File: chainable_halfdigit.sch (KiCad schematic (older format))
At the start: 42 parts, among them J1 Conn_01x03, J2 Conn_01x03

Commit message: Added more LEDs and created PCB
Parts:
- added C21, C22, C23: 100nF, Capacitors_SMD:C_0603, symbol C
- added LED21, LED22, LED23: WS2812B, WS2812B:WS2812B_data-bridgeable, symbol WS2812B
- C1, C10, C11, C12, C13, C14, C15, C16, C17, C18, C19, C2, C20, C3, C4, C5, C6, C7, C8, C9: footprint (none) -> Capacitors_SMD:C_0603
- J1, J2: footprint (none) -> Pin_Headers:Pin_Header_Straight_1x03_Pitch2.54mm
- LED1, LED10, LED11, LED12, LED13, LED14, LED15, LED16, LED17, LED18, LED19, LED2, LED20, LED3, LED4, LED5, LED6, LED7, LED8, LED9: footprint (none) -> WS2812B:WS2812B_data-bridgeable
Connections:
- net +5V: now also C21.1, C22.1, C23.1, LED21.1 (VCC), LED22.1 (VCC), LED23.1 (VCC)
- net DATA_OUT: now also LED23.2 (DOUT); no longer LED20.2 (DOUT)
- net GND: now also C21.2, C22.2, C23.2, LED21.3 (GND), LED22.3 (GND), LED23.3 (GND)
- new net: LED20.2 (DOUT), LED21.4 (DIN)
- new net: LED21.2 (DOUT), LED22.4 (DIN)
- new net: LED22.2 (DOUT), LED23.4 (DIN)
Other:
- moved on the sheet: C1, C10, C11, C12, C13, C14, C15, C16, C17, C18, C19, C2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

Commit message: Made pretty lib as local. Added 3D model to leds.
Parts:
- LED1, LED10, LED11, LED12, LED13, LED14, LED15, LED16, LED17, LED18, LED19, LED2, LED20, LED21, LED22, LED23, LED3, LED4, LED5, LED6, LED7, LED8, LED9: footprint WS2812B:WS2812B_data-bridgeable -> lib_fp:WS2812B_data-bridgeable
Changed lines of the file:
@@
 F 0 "LED1" H 1950 1050 60  0000 C CNN
 F 1 "WS2812B" H 1950 1850 60  0000 C CNN
-F 2 "WS2812B:WS2812B_data-bridgeable" V 1900 1450 60  0001 C CNN
+F 2 "lib_fp:WS2812B_data-bridgeable" V 1900 1450 60  0001 C CNN
 F 3 "" V 1900 1450 60  0000 C CNN
 	1    1950 1450
@@
 $EndComp
 $Comp
-L +5V #PWR2
+L +5V #PWR01
 U 1 1 5A021F2B
 P 1850 2250
-F 0 "#PWR2" H 1850 2100 50  0001 C CNN
+F 0 "#PWR01" H 1850 2100 50  0001 C CNN
 F 1 "+5V" H 1850 2390 50  0000 C CNN
 F 2 "" H 1850 2250 50  0001 C CNN
@@
 $EndComp
 $Comp
-L GND #PWR1
+L GND #PWR02
 U 1 1 5A021F41
 P 1450 750
-F 0 "#PWR1" H 1450 500 50  0001 C CNN
+F 0 "#PWR02" H 1450 500 50  0001 C CNN
 F 1 "GND" H 1450 600 50  0000 C CNN
 F 2 "" H 1450 750 50  0001 C CNN
@@
 F 0 "LED2" H 3150 1050 60  0000 C CNN
 F 1 "WS2812B" H 3150 1850 60  0000 C CNN
-F 2 "WS2812B:WS2812B_data-bridgeable" V 3100 1450 60  0001 C CNN
+F 2 "lib_fp:WS2812B_data-bridgeable" V 3100 1450 60  0001 C CNN
 F 3 "" V 3100 1450 60  0000 C CNN
 	1    3150 1450
@@
 F 0 "LED3" H 4350 1050 60  0000 C CNN
 F 1 "WS2812B" H 4350 1850 60  0000 C CNN
-F 2 "WS2812B:WS2812B_data-bridgeable" V 4300 1450 60  0001 C CNN
+F 2 "lib_fp:WS2812B_data-bridgeable" V 4300 1450 60  0001 C CNN
 F 3 "" V 4300 1450 60  0000 C CNN
 	1    4350 1450
@@
 F 0 "LED4" H 5550 1050 60  0000 C CNN
 F 1 "WS2812B" H 5550 1850 60  0000 C CNN
-F 2 "WS2812B:WS2812B_data-bridgeable" V 5500 1450 60  0001 C CNN
+F 2 "lib_fp:WS2812B_data-bridgeable" V 5500 1450 60  0001 C CNN
 F 3 "" V 5500 1450 60  0000 C CNN
 	1    5550 1450
@@
 F 0 "LED5" H 6750 1050 60  0000 C CNN
 F 1 "WS2812B" H 6750 1850 60  0000 C CNN
-F 2 "WS2812B:WS2812B_data-bridgeable" V 6700 1450 60  0001 C CNN
+F 2 "lib_fp:WS2812B_data-bridgeable" V 6700 1450 60  0001 C CNN
 F 3 "" V 6700 1450 60  0000 C CNN
 	1    6750 1450
@@
 F 0 "LED6" H 7950 1050 60  0000 C CNN
 F 1 "WS2812B" H 7950 1850 60  0000 C CNN
-F 2 "WS2812B:WS2812B_data-bridgeable" V 7900 1450 60  0001 C CNN
+F 2 "lib_fp:WS2812B_data-bridgeable" V 7900 1450 60  0001 C CNN
 F 3 "" V 7900 1450 60  0000 C CNN
 	1    7950 1450
@@
 F 0 "LED7" H 9150 1050 60  0000 C CNN
 F 1 "WS2812B" H 9150 1850 60  0000 C CNN
-F 2 "WS2812B:WS2812B_data-bridgeable" V 9100 1450 60  0001 C CNN
+F 2 "lib_fp:WS2812B_data-bridgeable" V 9100 1450 60  0001 C CNN
 F 3 "" V 9100 1450 60  0000 C CNN
 	1    9150 1450
@@
 F 0 "LED8" H 10350 1050 60  0000 C CNN
 F 1 "WS2812B" H 10350 1850 60  0000 C CNN
-F 2 "WS2812B:WS2812B_data-bridgeable" V 10300 1450 60  0001 C CNN
+F 2 "lib_fp:WS2812B_data-bridgeable" V 10300 1450 60  0001 C CNN
 F 3 "" V 10300 1450 60  0000 C CNN
 	1    10350 1450
@@
 F 0 "LED9" H 1950 3000 60  0000 C CNN
 F 1 "WS2812B" H 1950 3800 60  0000 C CNN
-F 2 "WS2812B:WS2812B_data-bridgeable" V 1900 3400 60  0001 C CNN
+F 2 "lib_fp:WS2812B_data-bridgeable" V 1900 3400 60  0001 C CNN
 F 3 "" V 1900 3400 60  0000 C CNN
 	1    1950 3400
@@
 F 0 "LED10" H 3150 3000 60  0000 C CNN
 F 1 "WS2812B" H 3150 3800 60  0000 C CNN
-F 2 "WS2812B:WS2812B_data-bridgeable" V 3100 3400 60  0001 C CNN
+F 2 "lib_fp:WS2812B_data-bridgeable" V 3100 3400 60  0001 C CNN
 F 3 "" V 3100 3400 60  0000 C CNN
 	1    3150 3400
@@
 F 0 "LED11" H 4350 3000 60  0000 C CNN
 F 1 "WS2812B" H 4350 3800 60  0000 C CNN
-F 2 "WS2812B:WS2812B_data-bridgeable" V 4300 3400 60  0001 C CNN
+F 2 "lib_fp:WS2812B_data-bridgeable" V 4300 3400 60  0001 C CNN
 F 3 "" V 4300 3400 60  0000 C CNN
 	1    4350 3400
@@
 F 0 "LED12" H 5550 3000 60  0000 C CNN
 F 1 "WS2812B" H 5550 3800 60  0000 C CNN
-F 2 "WS2812B:WS2812B_data-bridgeable" V 5500 3400 60  0001 C CNN
+F 2 "lib_fp:WS2812B_data-bridgeable" V 5500 3400 60  0001 C CNN
 F 3 "" V 5500 3400 60  0000 C CNN
 	1    5550 3400
@@
 F 0 "LED13" H 6750 3000 60  0000 C CNN
 F 1 "WS2812B" H 6750 3800 60  0000 C CNN
-F 2 "WS2812B:WS2812B_data-bridgeable" V 6700 3400 60  0001 C CNN
+F 2 "lib_fp:WS2812B_data-bridgeable" V 6700 3400 60  0001 C CNN
 F 3 "" V 6700 3400 60  0000 C CNN
 	1    6750 3400
@@
 F 0 "LED14" H 7950 3000 60  0000 C CNN
 F 1 "WS2812B" H 7950 3800 60  0000 C CNN
-F 2 "WS2812B:WS2812B_data-bridgeable" V 7900 3400 60  0001 C CNN
+F 2 "lib_fp:WS2812B_data-bridgeable" V 7900 3400 60  0001 C CNN
 F 3 "" V 7900 3400 60  0000 C CNN
 	1    7950 3400
@@
 F 0 "LED15" H 9150 3000 60  0000 C CNN
 F 1 "WS2812B" H 9150 3800 60  0000 C CNN
-F 2 "WS2812B:WS2812B_data-bridgeable" V 9100 3400 60  0001 C CNN
+F 2 "lib_fp:WS2812B_data-bridgeable" V 9100 3400 60  0001 C CNN
 F 3 "" V 9100 3400 60  0000 C CNN
 	1    9150 3400
@@
 F 0 "LED16" H 10350 3000 60  0000 C CNN
 F 1 "WS2812B" H 10350 3800 60  0000 C CNN
-F 2 "WS2812B:WS2812B_data-bridgeable" V 10300 3400 60  0001 C CNN
+F 2 "lib_fp:WS2812B_data-bridgeable" V 10300 3400 60  0001 C CNN
 F 3 "" V 10300 3400 60  0000 C CNN
 	1    10350 3400
@@
 F 0 "LED17" H 1950 4800 60  0000 C CNN
 F 1 "WS2812B" H 1950 5600 60  0000 C CNN
-F 2 "WS2812B:WS2812B_data-bridgeable" V 1900 5200 60  0001 C CNN
+F 2 "lib_fp:WS2812B_data-bridgeable" V 1900 5200 60  0001 C CNN
 F 3 "" V 1900 5200 60  0000 C CNN
 	1    1950 5200
@@
 F 0 "LED18" H 3150 4800 60  0000 C CNN
 F 1 "WS2812B" H 3150 5600 60  0000 C CNN
-F 2 "WS2812B:WS2812B_data-bridgeable" V 3100 5200 60  0001 C CNN
+F 2 "lib_fp:WS2812B_data-bridgeable" V 3100 5200 60  0001 C CNN
 F 3 "" V 3100 5200 60  0000 C CNN
 	1    3150 5200
@@
 F 0 "LED19" H 4350 4800 60  0000 C CNN
 F 1 "WS2812B" H 4350 5600 60  0000 C CNN
-F 2 "WS2812B:WS2812B_data-bridgeable" V 4300 5200 60  0001 C CNN
+F 2 "lib_fp:WS2812B_data-bridgeable" V 4300 5200 60  0001 C CNN
 F 3 "" V 4300 5200 60  0000 C CNN
 	1    4350 5200
@@
 F 0 "LED20" H 5550 4800 60  0000 C CNN
 F 1 "WS2812B" H 5550 5600 60  0000 C CNN
-F 2 "WS2812B:WS2812B_data-bridgeable" V 5500 5200 60  0001 C CNN
+F 2 "lib_fp:WS2812B_data-bridgeable" V 5500 5200 60  0001 C CNN
 F 3 "" V 5500 5200 60  0000 C CNN
 	1    5550 5200
@@
 DATA_INOUT_2
 $Comp
-L PWR_FLAG #FLG1
+L PWR_FLAG #FLG03
 U 1 1 5A02F033
 P 2650 750
-F 0 "#FLG1" H 2650 825 50  0001 C CNN
+F 0 "#FLG03" H 2650 825 50  0001 C CNN
 F 1 "PWR_FLAG" H 2650 900 50  0000 C CNN
 F 2 "" H 2650 750 50  0001 C CNN
@@
 $EndComp
 $Comp
-L PWR_FLAG #FLG2
+L PWR_FLAG #FLG04
 U 1 1 5A02F073
 P 1450 2250
-F 0 "#FLG2" H 1450 2325 50  0001 C CNN
+F 0 "#FLG04" H 1450 2325 50  0001 C CNN
 F 1 "PWR_FLAG" H 1450 2400 50  0000 C CNN
 F 2 "" H 1450 2250 50  0001 C CNN
@@
 F 0 "LED21" H 6750 4800 60  0000 C CNN
 F 1 "WS2812B" H 6750 5600 60  0000 C CNN
-F 2 "WS2812B:WS2812B_data-bridgeable" V 6700 5200 60  0001 C CNN
+F 2 "lib_fp:WS2812B_data-bridgeable" V 6700 5200 60  0001 C CNN
 F 3 "" V 6700 5200 60  0000 C CNN
 	1    6750 5200
@@
 F 0 "LED22" H 7950 4800 60  0000 C CNN
 F 1 "WS2812B" H 7950 5600 60  0000 C CNN
-F 2 "WS2812B:WS2812B_data-bridgeable" V 7900 5200 60  0001 C CNN
+F 2 "lib_fp:WS2812B_data-bridgeable" V 7900 5200 60  0001 C CNN
 F 3 "" V 7900 5200 60  0000 C CNN
 	1    7950 5200
@@
 F 0 "LED23" H 9150 4800 60  0000 C CNN
 F 1 "WS2812B" H 9150 5600 60  0000 C CNN
-F 2 "WS2812B:WS2812B_data-bridgeable" V 9100 5200 60  0001 C CNN
+F 2 "lib_fp:WS2812B_data-bridgeable" V 9100 5200 60  0001 C CNN
 F 3 "" V 9100 5200 60  0000 C CNN
 	1    9150 5200

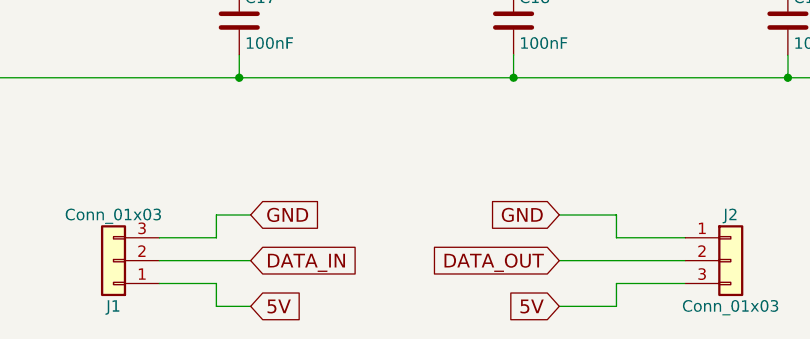
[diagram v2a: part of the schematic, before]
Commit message: Reverse 5V and DATA to avoid circuit damage when reversing connector.
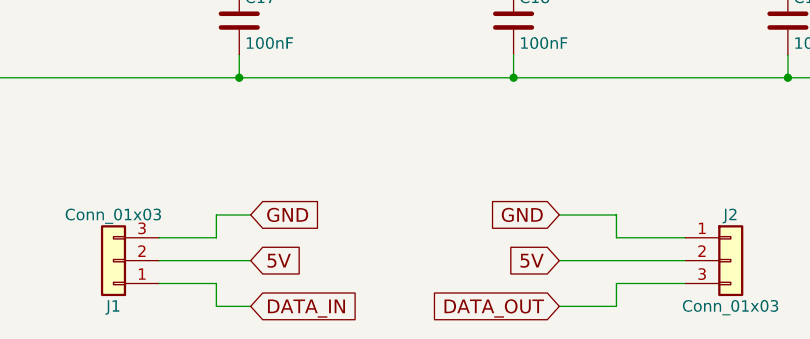
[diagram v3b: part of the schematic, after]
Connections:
- net +5V: now also J1.2 (Pin_2), J2.2 (Pin_2); no longer J1.1 (Pin_1), J2.3 (Pin_3)
- net DATA_IN: now also J1.1 (Pin_1); no longer J1.2 (Pin_2)
- net DATA_OUT: now also J2.3 (Pin_3); no longer J2.2 (Pin_2)
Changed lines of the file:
@@
 Text GLabel 2500 6850 2    60   Input ~ 0
 GND
+Text GLabel 2500 7050 2    60   Input ~ 0
+5V
 Text GLabel 2500 7250 2    60   Input ~ 0
-5V
-Text GLabel 2500 7050 2    60   Input ~ 0
 DATA_IN
 Text GLabel 1150 750  0    60   Input ~ 0
@@
 Text GLabel 3850 6850 0    60   Input ~ 0
 GND
+Text GLabel 3850 7250 0    60   Input ~ 0
+DATA_OUT
 Text GLabel 3850 7050 0    60   Input ~ 0
-DATA_OUT
-Text GLabel 3850 7250 0    60   Input ~ 0
 5V
 Text GLabel 1100 2850 0    60   Input ~ 0

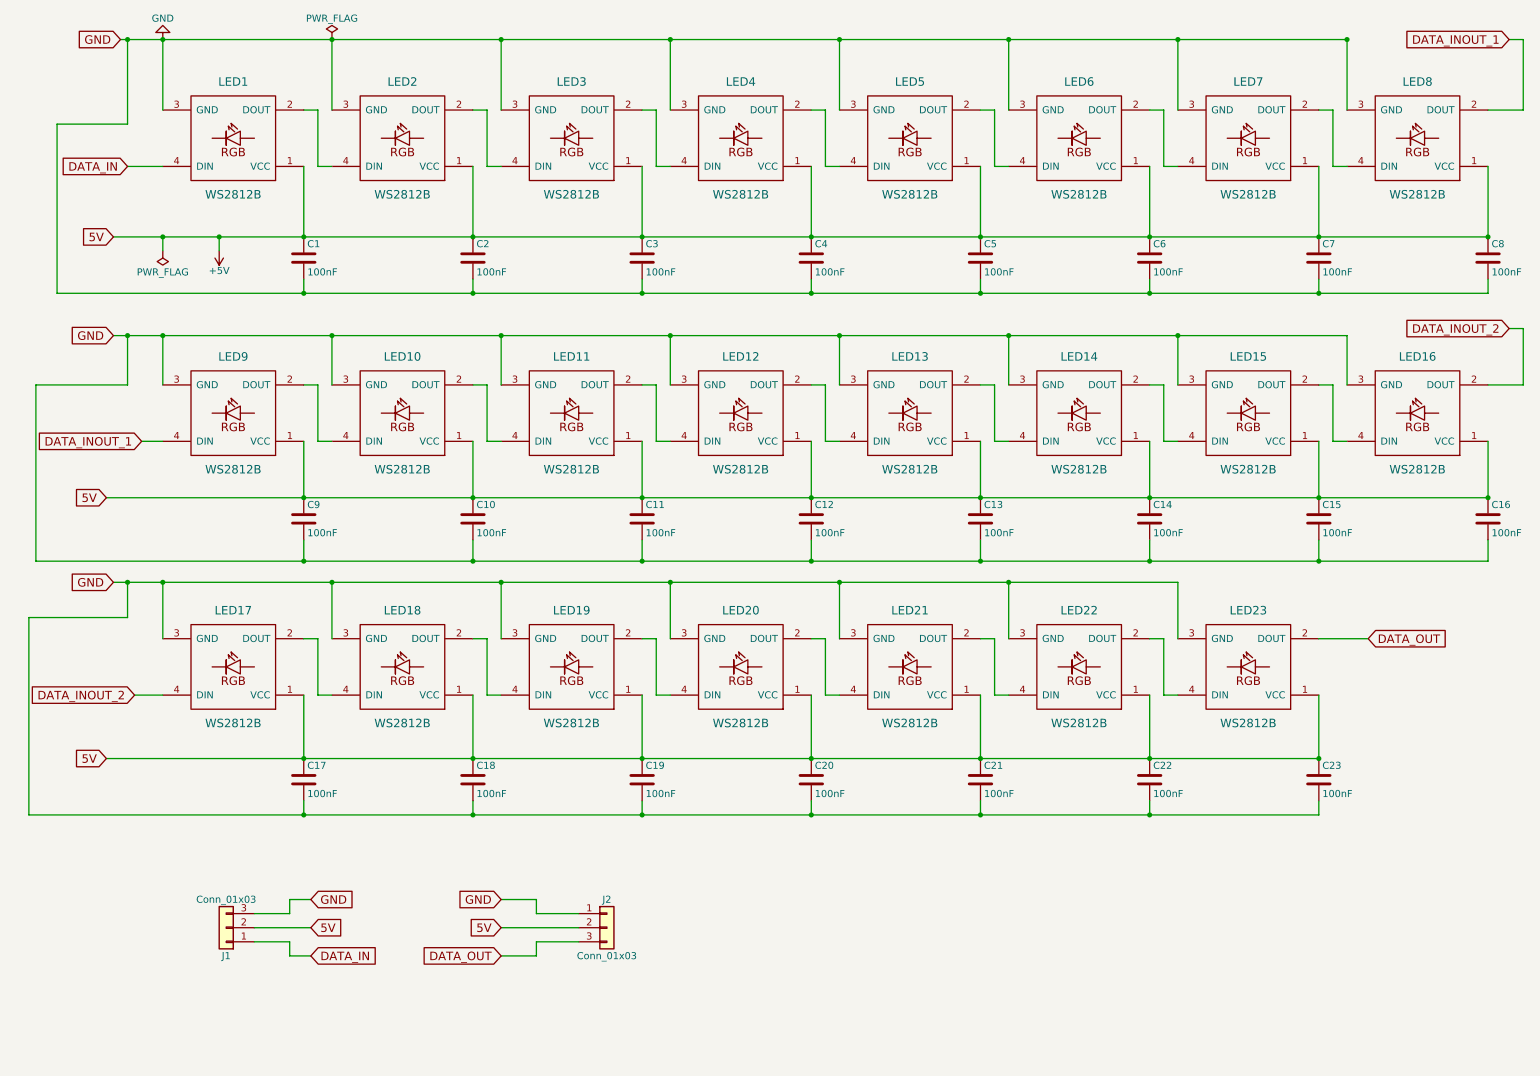
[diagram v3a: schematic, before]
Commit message: Added Arduino Nano footprint
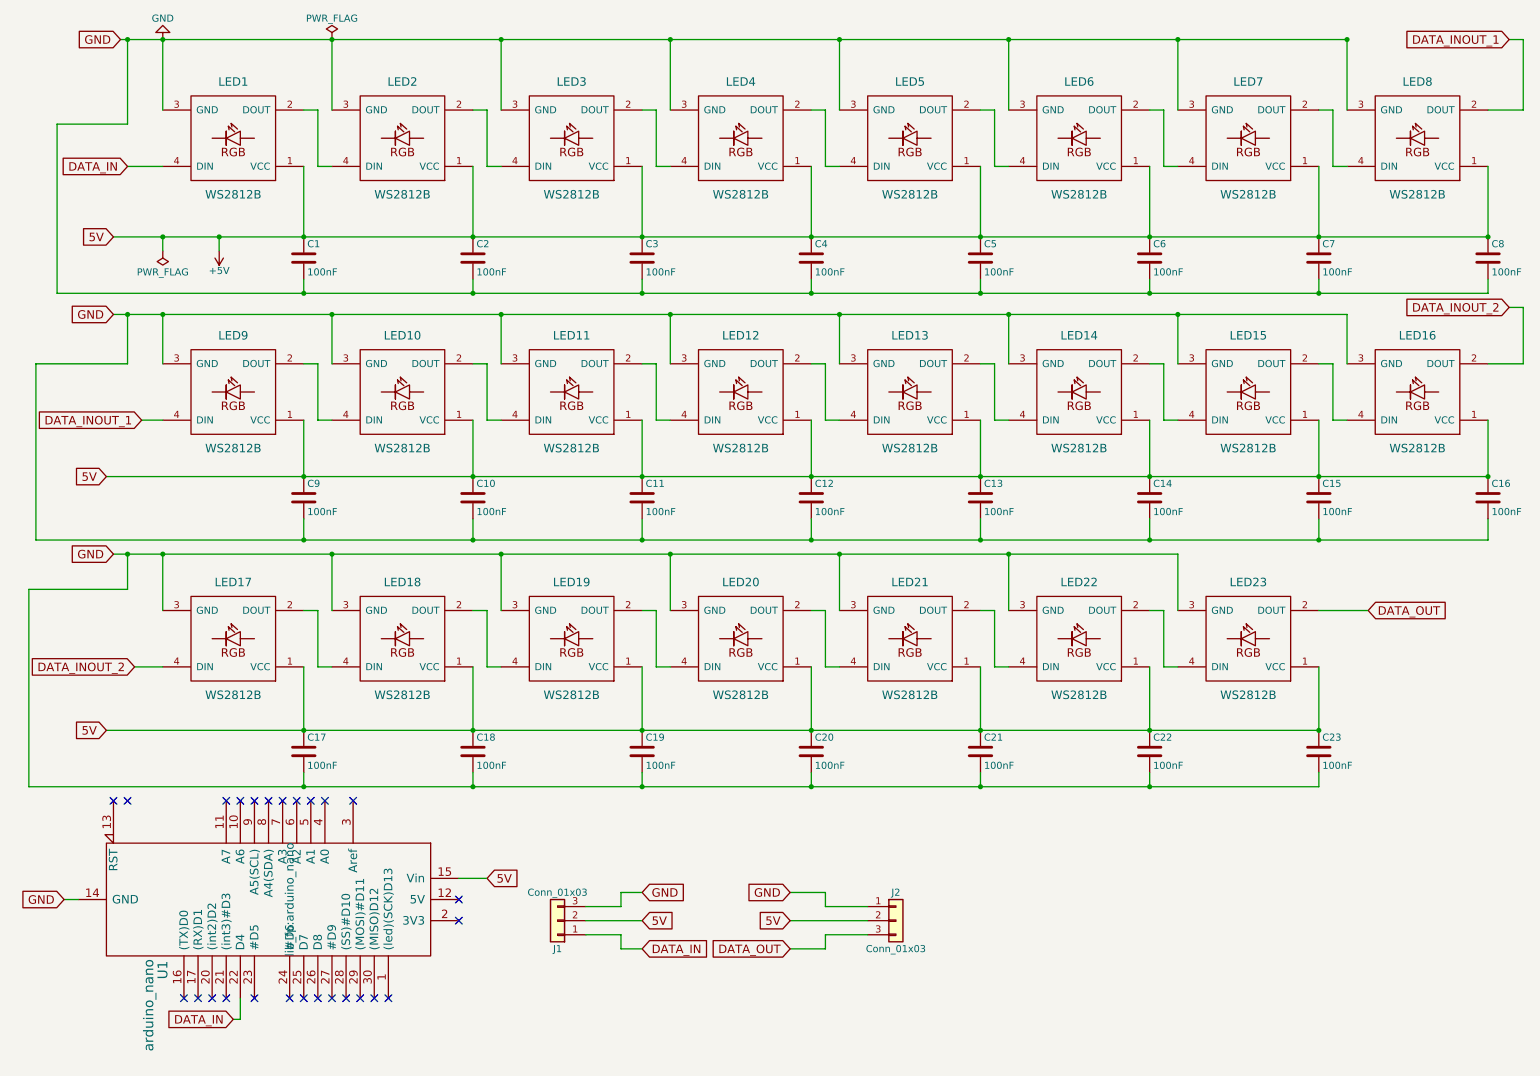
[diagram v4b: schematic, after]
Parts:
- added U1: arduino_nano, lib_fp:arduino_nano, symbol arduino_nano
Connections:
- net +5V: now also U1.15 (Vin)
- net DATA_IN: now also U1.22 (D4)
- net GND: now also U1.14 (GND), U1.19 (GND)
- no-connect marks 0 -> 26
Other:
- moved on the sheet: C10, C11, C12, C13, C14, C15, C16, C17, C18, C19, C20, C21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

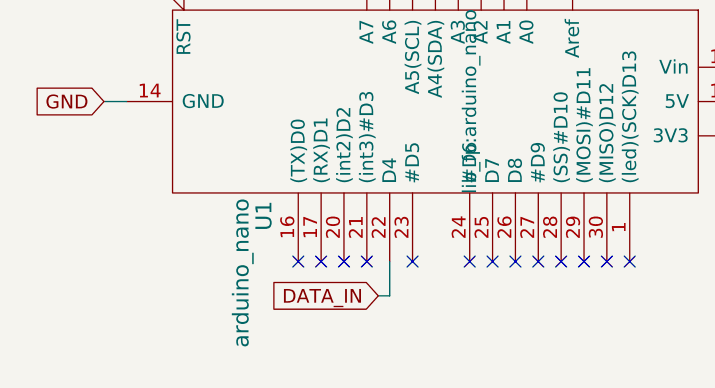
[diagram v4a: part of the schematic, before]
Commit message: Changed DATA_IN in arduino nano from D4 to D3. Moved some components.
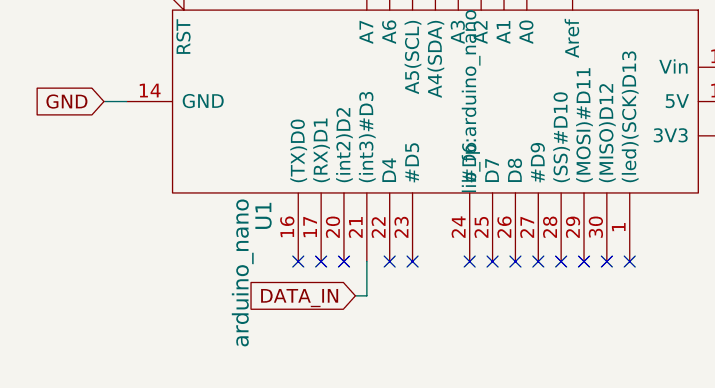
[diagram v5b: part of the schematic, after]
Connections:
- net DATA_IN: now also U1.21 ((int3)#D3); no longer U1.22 (D4)
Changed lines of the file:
@@
 LIBS:ws2812b
 LIBS:arduino
-LIBS:nRF24L01+
 LIBS:power
 LIBS:device
@@
 Wire Wire Line
 	750  6850 850  6850
-Text GLabel 1950 7700 0    60   Input ~ 0
+Text GLabel 1850 7700 0    60   Input ~ 0
 DATA_IN
-Wire Wire Line
-	2000 7550 2000 7700
-Wire Wire Line
-	2000 7700 1950 7700
 NoConn ~ 1100 6150
 NoConn ~ 1900 6150
@@
 NoConn ~ 1700 7550
 NoConn ~ 1800 7550
-NoConn ~ 1900 7550
+NoConn ~ 2000 7550
 NoConn ~ 2100 7550
 NoConn ~ 2350 7550
@@
 NoConn ~ 3550 7000
 NoConn ~ 1200 6150
+Wire Wire Line
+	1850 7700 1900 7700
+Wire Wire Line
+	1900 7700 1900 7550
 $EndSCHEMATC
